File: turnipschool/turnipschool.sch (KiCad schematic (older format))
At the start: 60 parts, among them J1 USB-DEVICE-SHIELD, P1 CONN_1, P2 RESET_N, P3 DD, P4 DC, P5 3V3, P6 GND, P7 CABLE, T1 BALUN, U1 CC1111, U2 AP7313, U3 USB2412, U4 AP2511SN-7, U5 AH1806, X1 GSG-XTAL4PIN, X2 GSG-XTAL4PIN

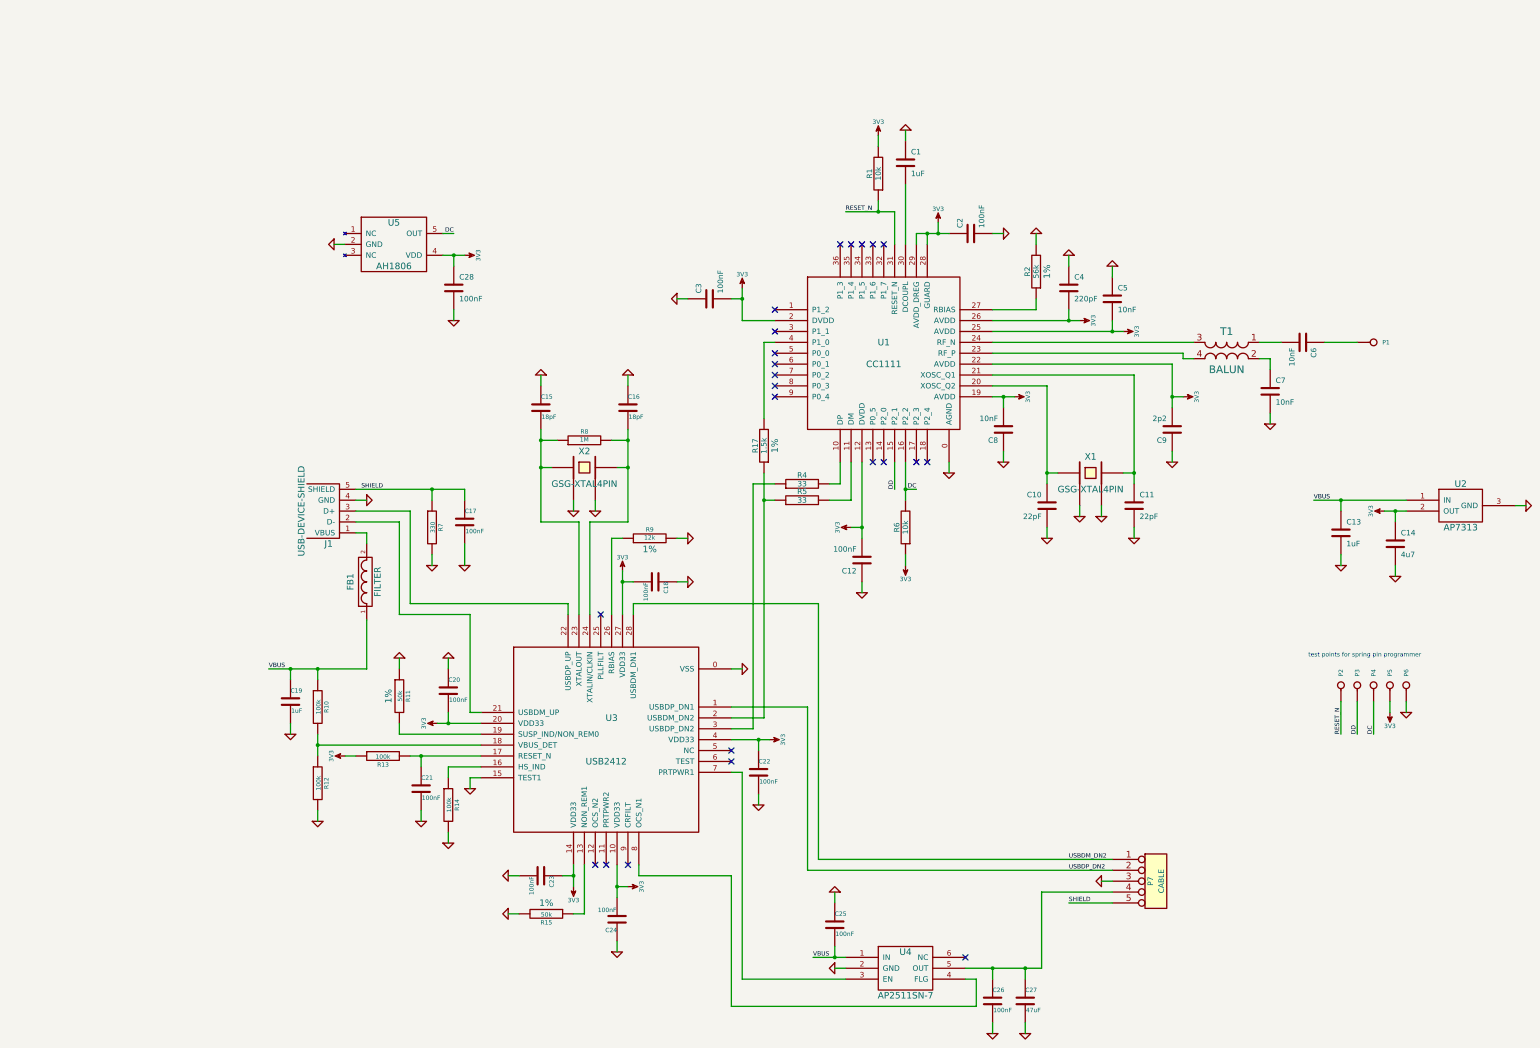
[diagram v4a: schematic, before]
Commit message: reworked layout so USB traces have contiguous zones beneath them
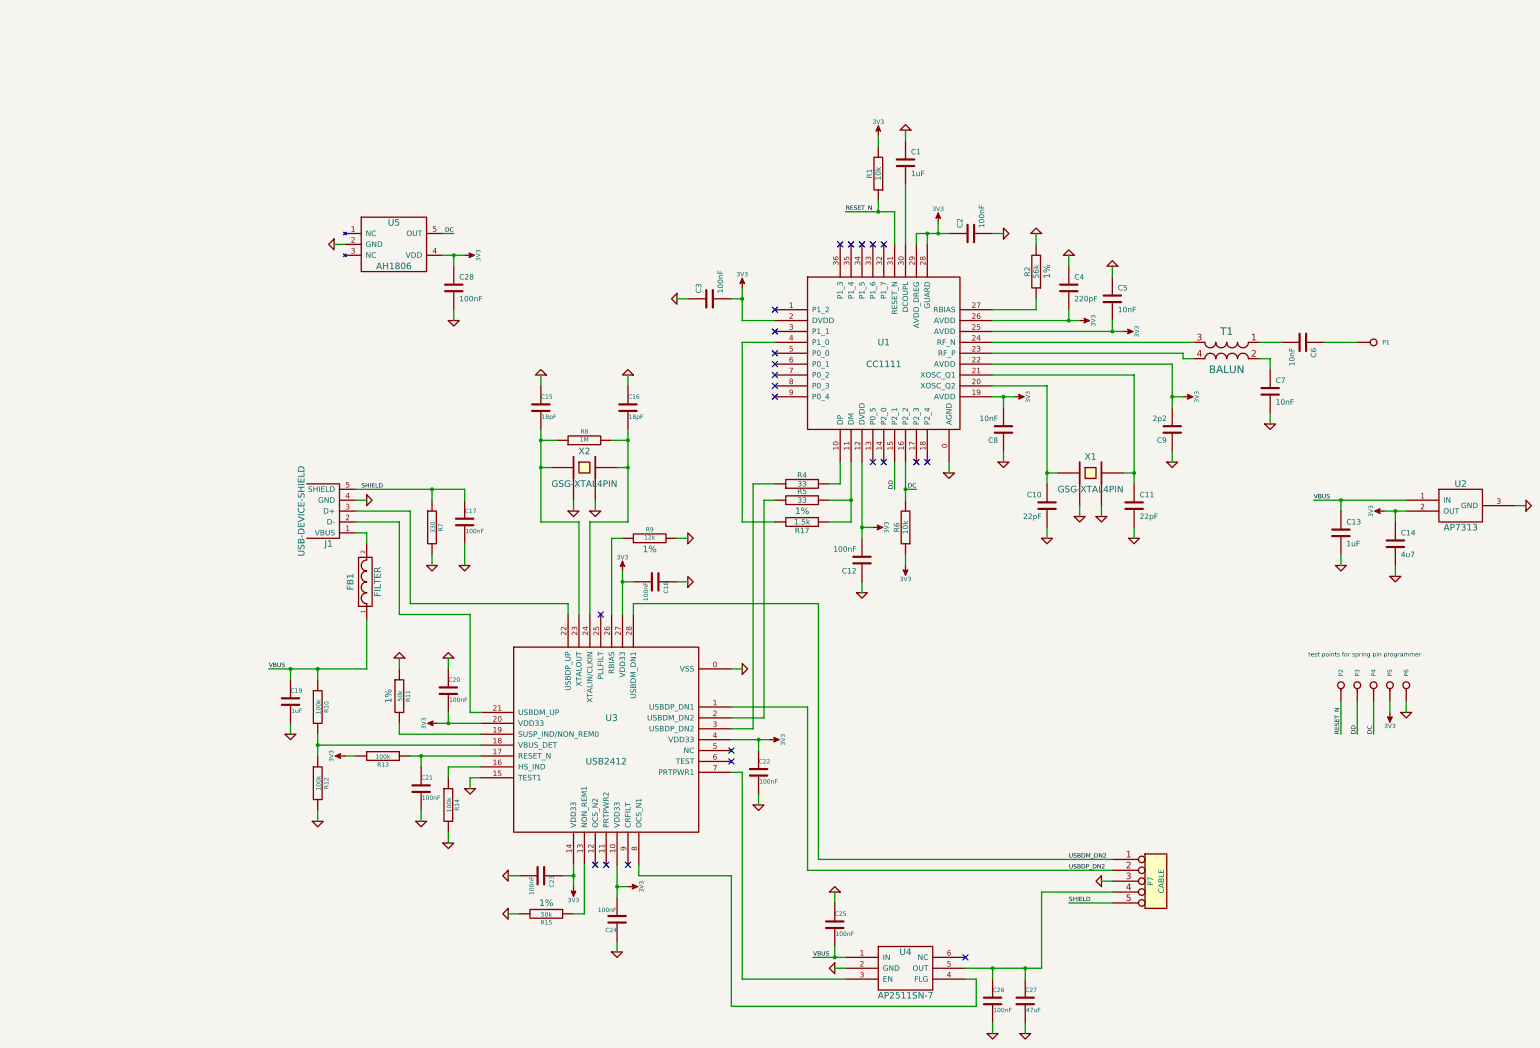
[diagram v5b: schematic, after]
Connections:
- net at R5.1, U3.2 (USBDM_DN2): no longer R17.1
- net at R5.2, U1.11 (DM): now also R17.1
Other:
- moved on the sheet: R17
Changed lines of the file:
@@
 L 3V3 #PWR08
 U 1 1 504D0F27
-P 8400 5300
-F 0 "#PWR08" H 8400 5400 40  0001 C CNN
-F 1 "3V3" H 8400 5425 40  0000 C CNN
-F 2 "" H 8400 5300 60  0001 C CNN
-F 3 "" H 8400 5300 60  0001 C CNN
-	1    8400 5300
-	0    -1   -1   0
+P 8600 5300
+F 0 "#PWR08" H 8600 5400 40  0001 C CNN
+F 1 "3V3" H 8600 5425 40  0000 C CNN
+F 2 "" H 8600 5300 60  0001 C CNN
+F 3 "" H 8600 5300 60  0001 C CNN
+	1    8600 5300
+	0    1    1    0
 $EndComp
 $Comp
@@
 $EndComp
 $Comp
-L 3V3 #PWR059
+L 3V3 #PWR058
 U 1 1 548DEB3A
 P 4850 2800
-F 0 "#PWR059" H 4850 2900 40  0001 C CNN
+F 0 "#PWR058" H 4850 2900 40  0001 C CNN
 F 1 "3V3" H 4850 2925 40  0000 C CNN
 F 2 "" H 4850 2800 60  0001 C CNN
@@
 $EndComp
 $Comp
-L GND #PWR060
+L GND #PWR059
 U 1 1 548DEFB8
 P 4750 3400
-F 0 "#PWR060" H 4750 3400 30  0001 C CNN
+F 0 "#PWR059" H 4750 3400 30  0001 C CNN
 F 1 "GND" H 4750 3330 30  0001 C CNN
 F 2 "" H 4750 3400 60  0000 C CNN
@@
 NoConn ~ 8700 2700
 $Comp
-L GND #PWR061
+L GND #PWR060
 U 1 1 548F49A4
 P 6900 5800
-F 0 "#PWR061" H 6900 5800 30  0001 C CNN
+F 0 "#PWR060" H 6900 5800 30  0001 C CNN
 F 1 "GND" H 6900 5730 30  0001 C CNN
 F 2 "" H 6900 5800 60  0000 C CNN
@@
 	4750 2800 4750 2900
 Wire Wire Line
-	4650 2800 4750 2800
-Wire Wire Line
-	4750 2800 4850 2800
+	4650 2800 4850 2800
 Wire Wire Line
 	7300 6600 7400 6600
@@
 	12900 6900 12900 7200
 Wire Wire Line
-	12650 5050 12900 5050
-Wire Wire Line
-	12900 5050 13500 5050
+	12650 5050 13500 5050
 Connection ~ 8650 2400
 Wire Wire Line
-	8350 2400 8650 2400
-Wire Wire Line
-	8650 2400 8800 2400
+	8350 2400 8800 2400
 Connection ~ 12900 5050
 Wire Wire Line
@@
 Connection ~ 13400 5150
 Wire Wire Line
-	13300 5150 13400 5150
-Wire Wire Line
-	13400 5150 13500 5150
-Wire Wire Line
-	9700 3400 10400 3400
-Wire Wire Line
-	10400 3400 10500 3400
+	13300 5150 13500 5150
+Wire Wire Line
+	9700 3400 10500 3400
 Wire Wire Line
 	11350 4700 11350 4600
 Wire Wire Line
-	11350 3800 11350 4100
-Wire Wire Line
-	11350 4100 11350 4200
-Wire Wire Line
-	10200 4000 10200 4800
-Wire Wire Line
-	10200 4800 10200 4900
+	11350 3800 11350 4200
+Wire Wire Line
+	10200 4000 10200 4900
 Wire Wire Line
 	10200 4000 9700 4000
@@
 	9200 2600 9200 2500
 Wire Wire Line
-	9000 2600 9100 2600
-Wire Wire Line
-	9100 2600 9200 2600
-Wire Wire Line
-	9200 2600 9300 2600
+	9000 2600 9300 2600
 Wire Wire Line
 	9000 2600 9000 2700
@@
 	11450 3750 11550 3750
 Wire Wire Line
-	9700 4100 9800 4100
-Wire Wire Line
-	9800 4100 9900 4100
+	9700 4100 9900 4100
 Wire Wire Line
 	10300 4800 10200 4800
@@
 	8500 5900 8500 5800
 Wire Wire Line
-	8400 5300 8500 5300
-Wire Wire Line
-	8500 4700 8500 5300
-Wire Wire Line
-	8500 5300 8500 5400
+	8500 4700 8500 5400
 Connection ~ 8500 5300
 Wire Wire Line
@@
 	10800 2900 10800 3000
 Wire Wire Line
-	9700 3500 10800 3500
-Wire Wire Line
-	10800 3500 10900 3500
+	9700 3500 10900 3500
 Wire Wire Line
 	10800 3400 10800 3500
@@
 	7300 3200 7400 3200
 Wire Wire Line
-	7400 3100 7400 3200
-Wire Wire Line
-	7400 3200 7400 3400
+	7400 3100 7400 3400
 Wire Wire Line
 	7400 3400 7700 3400
@@
 	8800 2400 8800 2700
 Wire Wire Line
-	8400 4700 8400 5050
+	8400 4700 8400 5250
 Wire Wire Line
 	8400 5050 8200 5050
@@
 	8350 9350 8250 9350
 Wire Wire Line
-	8050 9250 8250 9250
-Wire Wire Line
-	8250 9250 8350 9250
+	8050 9250 8350 9250
 Wire Wire Line
 	5000 7500 4700 7500
@@
 	4250 6600 4250 6500
 Wire Wire Line
-	4350 7400 4450 7400
-Wire Wire Line
-	4450 7400 5000 7400
+	4350 7400 5000 7400
 Wire Wire Line
 	4450 7500 4450 7400
@@
 	5000 7300 3500 7300
 Wire Wire Line
-	3500 7200 3500 7300
-Wire Wire Line
-	3500 7300 3500 7400
+	3500 7200 3500 7400
 Connection ~ 3500 7300
 Wire Wire Line
@@
 	5550 4000 5550 3900
 Wire Wire Line
-	9450 9350 9700 9350
-Wire Wire Line
-	9700 9350 10000 9350
-Wire Wire Line
-	10000 9350 10150 9350
+	9450 9350 10150 9350
 Wire Wire Line
 	12750 3600 13050 3600
 Wire Wire Line
-	8900 4700 8900 4950
-Wire Wire Line
-	8900 4950 8900 5050
+	8900 4700 8900 5050
 Wire Wire Line
 	13350 6900 13350 7000
 Wire Wire Line
-	3850 4950 4550 4950
-Wire Wire Line
-	4550 4950 4850 4950
+	3850 4950 4850 4950
 Wire Wire Line
 	3950 5050 3850 5050
@@
 Connection ~ 8250 9250
 Wire Wire Line
-	4600 7100 4700 7100
-Wire Wire Line
-	4700 7100 5000 7100
-Wire Wire Line
-	6300 5700 6300 5800
-Wire Wire Line
-	6300 5800 6300 6100
-Wire Wire Line
-	6250 8400 6250 8600
-Wire Wire Line
-	6250 8600 6250 8700
+	4600 7100 5000 7100
+Wire Wire Line
+	6300 5700 6300 6100
+Wire Wire Line
+	6250 8400 6250 8700
 Connection ~ 9700 9350
 Wire Wire Line
@@
 	10000 9350 10000 9450
 Wire Wire Line
-	11000 3900 11000 4800
-Wire Wire Line
-	11000 4800 11000 4900
+	11000 3900 11000 4900
 Wire Wire Line
 	11000 3900 9700 3900
@@
 	10700 8550 10800 8550
 Wire Wire Line
-	6350 4400 6350 4500
-Wire Wire Line
-	6350 4500 6350 4750
-Wire Wire Line
-	6350 4750 6350 5250
+	6350 4400 6350 5250
 Wire Wire Line
 	6350 5250 6000 5250
@@
 	6000 5250 6000 6100
 Wire Wire Line
-	5550 4400 5550 4500
-Wire Wire Line
-	5550 4500 5550 4750
-Wire Wire Line
-	5550 4750 5550 5250
+	5550 4400 5550 5250
 Wire Wire Line
 	5550 5250 5900 5250
@@
 	3250 6700 3250 6600
 Wire Wire Line
-	3050 6600 3250 6600
-Wire Wire Line
-	3250 6600 3500 6600
-Wire Wire Line
-	3500 6600 3950 6600
+	3050 6600 3950 6600
 Wire Wire Line
 	3500 6600 3500 6700
@@
 Connection ~ 4700 7100
 $Comp
-L GND #PWR062
+L GND #PWR061
 U 1 1 548F80B7
 P 4700 6500
-F 0 "#PWR062" H 4700 6500 30  0001 C CNN
+F 0 "#PWR061" H 4700 6500 30  0001 C CNN
 F 1 "GND" H 4700 6430 30  0001 C CNN
 F 2 "" H 4700 6500 60  0001 C CNN
@@
 	4250 7200 4250 7100
 $Comp
-L GND #PWR063
+L GND #PWR062
 U 1 1 548F92E8
 P 7550 7850
-F 0 "#PWR063" H 7550 7850 30  0001 C CNN
+F 0 "#PWR062" H 7550 7850 30  0001 C CNN
 F 1 "GND" H 7550 7780 30  0001 C CNN
 F 2 "" H 7550 7850 60  0000 C CNN
@@
 	7550 7750 7550 7850
 Wire Wire Line
-	7300 7250 7550 7250
-Wire Wire Line
-	7550 7250 7650 7250
+	7300 7250 7650 7250
 Wire Wire Line
 	7550 7250 7550 7350
@@
 Connection ~ 6250 8600
 $Comp
-L GND #PWR064
+L GND #PWR063
 U 1 1 548FB44A
 P 6250 9200
-F 0 "#PWR064" H 6250 9200 30  0001 C CNN
+F 0 "#PWR063" H 6250 9200 30  0001 C CNN
 F 1 "GND" H 6250 9130 30  0001 C CNN
 F 2 "" H 6250 9200 60  0001 C CNN
@@
 $EndComp
 Wire Wire Line
-	5850 8400 5850 8500
-Wire Wire Line
-	5850 8500 5850 8600
+	5850 8400 5850 8600
 Wire Wire Line
 	5850 8500 5750 8500
 Connection ~ 5850 8500
 $Comp
-L GND #PWR065
+L GND #PWR064
 U 1 1 548FBE98
 P 5250 8500
-F 0 "#PWR065" H 5250 8500 30  0001 C CNN
+F 0 "#PWR064" H 5250 8500 30  0001 C CNN
 F 1 "GND" H 5250 8430 30  0001 C CNN
 F 2 "" H 5250 8500 60  0001 C CNN
@@
 L R R17
 U 1 1 549012D7
-P 7600 4550
-F 0 "R17" V 7680 4550 50  0000 C CNN
-F 1 "1.5k" V 7600 4550 50  0000 C CNN
-F 2 "cc1111-legacy:GSG-0402" H 7600 4550 60  0001 C CNN
-F 3 "" H 7600 4550 60  0001 C CNN
-F 4 "Rohm" H 7600 4550 60  0001 C CNN "Manufacturer"
-F 5 "MCR03ERTF1501" H 7600 4550 60  0001 C CNN "Part Number"
-F 6 "RES 1.50K OHM 1/10W 1% 0603 SMD" H 7600 4550 60  0001 C CNN "Description"
-F 7 "1%" V 7500 4550 60  0000 C CNN "Note"
-	1    7600 4550
-	-1   0    0    1
-$EndComp
-Connection ~ 7600 5050
-Wire Wire Line
-	7700 3600 7600 3600
-Wire Wire Line
-	7600 3600 7600 4300
+P 7950 5250
+F 0 "R17" V 8030 5250 50  0000 C CNN
+F 1 "1.5k" V 7950 5250 50  0000 C CNN
+F 2 "cc1111-legacy:GSG-0402" H 7950 5250 60  0001 C CNN
+F 3 "" H 7950 5250 60  0001 C CNN
+F 4 "Rohm" H 7950 5250 60  0001 C CNN "Manufacturer"
+F 5 "MCR03ERTF1501" H 7950 5250 60  0001 C CNN "Part Number"
+F 6 "RES 1.50K OHM 1/10W 1% 0603 SMD" H 7950 5250 60  0001 C CNN "Description"
+F 7 "1%" V 7850 5250 60  0000 C CNN "Note"
+	1    7950 5250
+	0    1    1    0
+$EndComp
 NoConn ~ 7700 3500
-Wire Wire Line
-	7600 4800 7600 5050
-Wire Wire Line
-	7600 5050 7600 7050
 Wire Wire Line
 	7600 7050 7300 7050
@@
 NoConn ~ 6150 8400
 $Comp
-L GND #PWR066
+L GND #PWR065
 U 1 1 5490A6E9
 P 4250 6500
-F 0 "#PWR066" H 4250 6500 30  0001 C CNN
+F 0 "#PWR065" H 4250 6500 30  0001 C CNN
 F 1 "GND" H 4250 6430 30  0001 C CNN
 F 2 "" H 4250 6500 60  0001 C CNN
@@
 DC
 NoConn ~ 8600 2700
+Wire Wire Line
+	8500 5300 8600 5300
+Wire Wire Line
+	8400 5250 8200 5250
+Connection ~ 8400 5050
+Wire Wire Line
+	7600 5050 7600 7050
+Wire Wire Line
+	7700 5250 7400 5250
+Wire Wire Line
+	7400 5250 7400 3600
+Wire Wire Line
+	7400 3600 7700 3600
 $EndSCHEMATC

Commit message: bom update
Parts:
- C14: Description CAP CER 4.7UF 6.3V 20% X5R 0402 -> CAP CER 4.7UF 6.3V 20% X5R 0402
- C6: Description CAP CER 10000PF 16V 10% X7R 0402 -> CAP CER 10000PF 25V 10% X7R 0402; Manufacturer Samsung Electro-Mechanics America, Inc -> Murata; Part Number CL05B103KO5NCNC -> GRM155R71E103KA01D
- C9: Part Number GRM1555C1H2R2CZ01D -> GRM1555C1H2R2CA01D
- P1, P7: Note (none) -> DNP
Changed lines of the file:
@@
 F 2 "cc1111-legacy:GSG-0402" H 12550 3600 60  0001 C CNN
 F 3 "" H 12550 3600 60  0001 C CNN
-F 4 "Samsung Electro-Mechanics America, Inc" H 12550 3600 60  0001 C CNN "Manufacturer"
-F 5 "CL05B103KO5NCNC" H 12550 3600 60  0001 C CNN "Part Number"
-F 6 "CAP CER 10000PF 16V 10% X7R 0402" H 12550 3600 60  0001 C CNN "Description"
+F 4 "Murata" H 12550 3600 60  0001 C CNN "Manufacturer"
+F 5 "GRM155R71E103KA01D" H 12550 3600 60  0001 C CNN "Part Number"
+F 6 "CAP CER 10000PF 25V 10% X7R 0402" H 12550 3600 60  0001 C CNN "Description"
 	1    12550 3600
 	0    1    1    0
@@
 F 4 "Samsung Electro-Mechanics America, Inc" H 13400 5450 60  0001 C CNN "Manufacturer"
 F 5 "CL05A475MQ5NRNC" H 13400 5450 60  0001 C CNN "Part Number"
-F 6 "	CAP CER 4.7UF 6.3V 20% X5R 0402" H 13400 5450 60  0001 C CNN "Description"
+F 6 "CAP CER 4.7UF 6.3V 20% X5R 0402" H 13400 5450 60  0001 C CNN "Description"
 	1    13400 5450
 	1    0    0    -1
@@
 F 3 "" H 11350 4400 60  0001 C CNN
 F 4 "Murata" H 11350 4400 60  0001 C CNN "Manufacturer"
-F 5 "GRM1555C1H2R2CZ01D" H 11350 4400 60  0001 C CNN "Part Number"
+F 5 "GRM1555C1H2R2CA01D" H 11350 4400 60  0001 C CNN "Part Number"
 F 6 "CAP CER 2.2PF 50V NP0 0402" H 11350 4400 60  0001 C CNN "Description"
 	1    11350 4400
@@
 F 2 "cc1111-legacy:GSG-50MIL-HEADER-1x1-TH" H 13200 3600 60  0001 C CNN
 F 3 "" H 13200 3600 60  0001 C CNN
+F 4 "DNP" H 13200 3600 60  0001 C CNN "Note"
 	1    13200 3600
 	1    0    0    -1
@@
 F 2 "cc1111-legacy:GSG-50MIL-HEADER-1x5-TH" H 11200 8550 60  0001 C CNN
 F 3 "" H 11200 8550 60  0001 C CNN
+F 4 "DNP" V 11200 8550 60  0001 C CNN "Note"
 	1    11200 8550
 	1    0    0    -1

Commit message: corrected USB connector BOM info
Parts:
- J1: Description CONN PLUG USB A-TYPE SMD -> CONN USB A TYPE ULTRA FLAT T/H; Manufacturer Keystone Electronics -> CNC Tech; Part Number 931 -> 1001-010-01001
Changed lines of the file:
@@
 F 2 "cc1111-legacy:GSG-USB-A-1001-010-01001-SHIELD" H 3650 5150 60  0001 C CNN
 F 3 "" H 3650 5150 60  0001 C CNN
-F 4 "Keystone Electronics" H 3650 5150 60  0001 C CNN "Manufacturer"
-F 5 "931" H 3650 5150 60  0001 C CNN "Part Number"
-F 6 "CONN PLUG USB A-TYPE SMD" H 3650 5150 60  0001 C CNN "Description"
+F 4 "CNC Tech" H 3650 5150 60  0001 C CNN "Manufacturer"
+F 5 "1001-010-01001" H 3650 5150 60  0001 C CNN "Part Number"
+F 6 "CONN USB A TYPE ULTRA FLAT T/H" H 3650 5150 60  0001 C CNN "Description"
 	1    3650 5150
 	-1   0    0    1

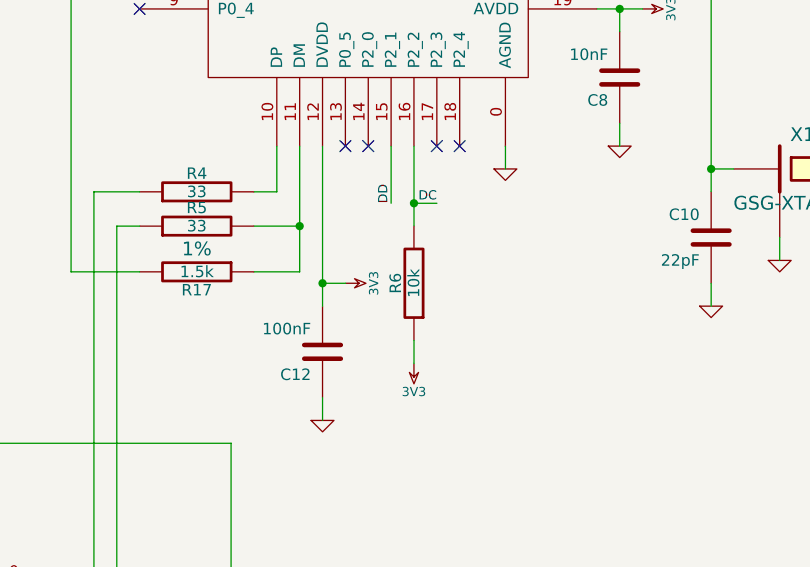
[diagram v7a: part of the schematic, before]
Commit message: changed R6 from 10k to 100k for improved reliability of magnetic sensor bootloader activation
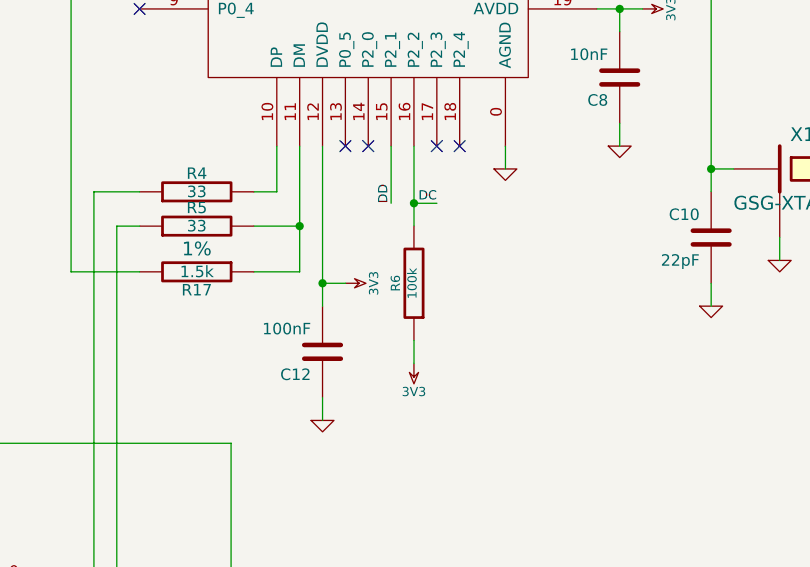
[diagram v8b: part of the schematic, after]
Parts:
- R6: value 10k -> 100k; Description RES 10.0K OHM 1/16W 5% 0402 -> RES 100K OHM 1/16W 5% 0402; Manufacturer TE Connectivity -> Samsung Electro-Mechanics America, Inc; Part Number 1622826-4 -> RC1005J104CS
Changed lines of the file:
@@
-$EndComp
-$Comp
-L R R6
-U 1 1 504CF38E
-P 8900 5300
-F 0 "R6" V 8980 5300 50  0000 C CNN
-F 1 "10k" V 8900 5300 50  0000 C CNN
-F 2 "cc1111-legacy:GSG-0402" H 8900 5300 60  0001 C CNN
-F 3 "" H 8900 5300 60  0001 C CNN
-F 4 "TE Connectivity" H 8900 5300 60  0001 C CNN "Manufacturer"
-F 5 "1622826-4" H 8900 5300 60  0001 C CNN "Part Number"
-F 6 "RES 10.0K OHM 1/16W 5% 0402" H 8900 5300 60  0001 C CNN "Description"
-	1    8900 5300
-	-1   0    0    1
 $EndComp
 $Comp
@@
 Wire Wire Line
 	7400 3600 7700 3600
+$Comp
+L R R6
+U 1 1 54C7D1D6
+P 8900 5300
+F 0 "R6" V 8980 5300 40  0000 C CNN
+F 1 "100k" V 8907 5301 40  0000 C CNN
+F 2 "cc1111-legacy:GSG-0402" H 8900 5300 60  0001 C CNN
+F 3 "" H 8900 5300 60  0001 C CNN
+F 4 "Samsung Electro-Mechanics America, Inc" H 8900 5300 60  0001 C CNN "Manufacturer"
+F 5 "RC1005J104CS" H 8900 5300 60  0001 C CNN "Part Number"
+F 6 "RES 100K OHM 1/16W 5% 0402" H 8900 5300 60  0001 C CNN "Description"
+	1    8900 5300
+	-1   0    0    1
+$EndComp
 $EndSCHEMATC
